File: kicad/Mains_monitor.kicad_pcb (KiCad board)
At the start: 2 copper layers, 69 x 89 mm, 35 parts, among them J1 Screw_Terminal_01x02, J2 Screw_Terminal_01x02, K1 SANYOU_SRD_Form_C, Q1 NPN, U1 HLW8032

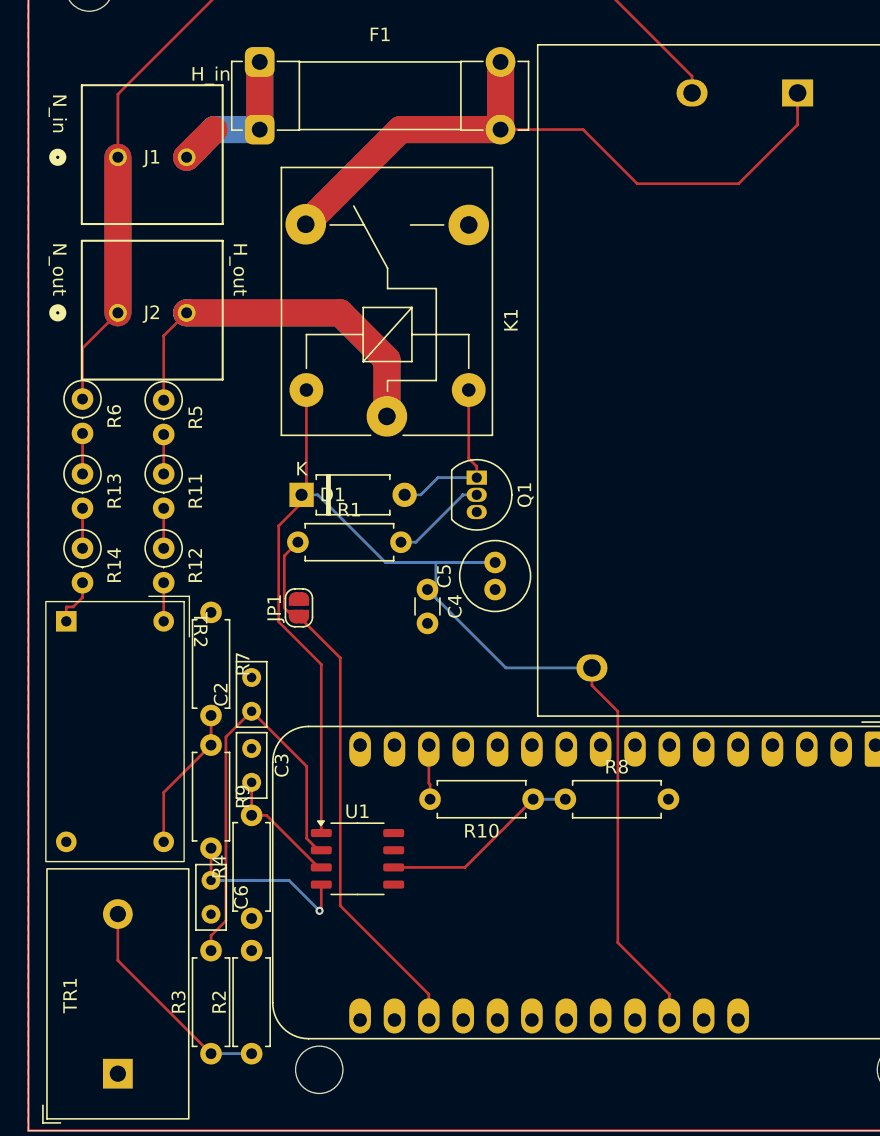
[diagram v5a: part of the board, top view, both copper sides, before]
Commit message: added updated screw terminal footprints
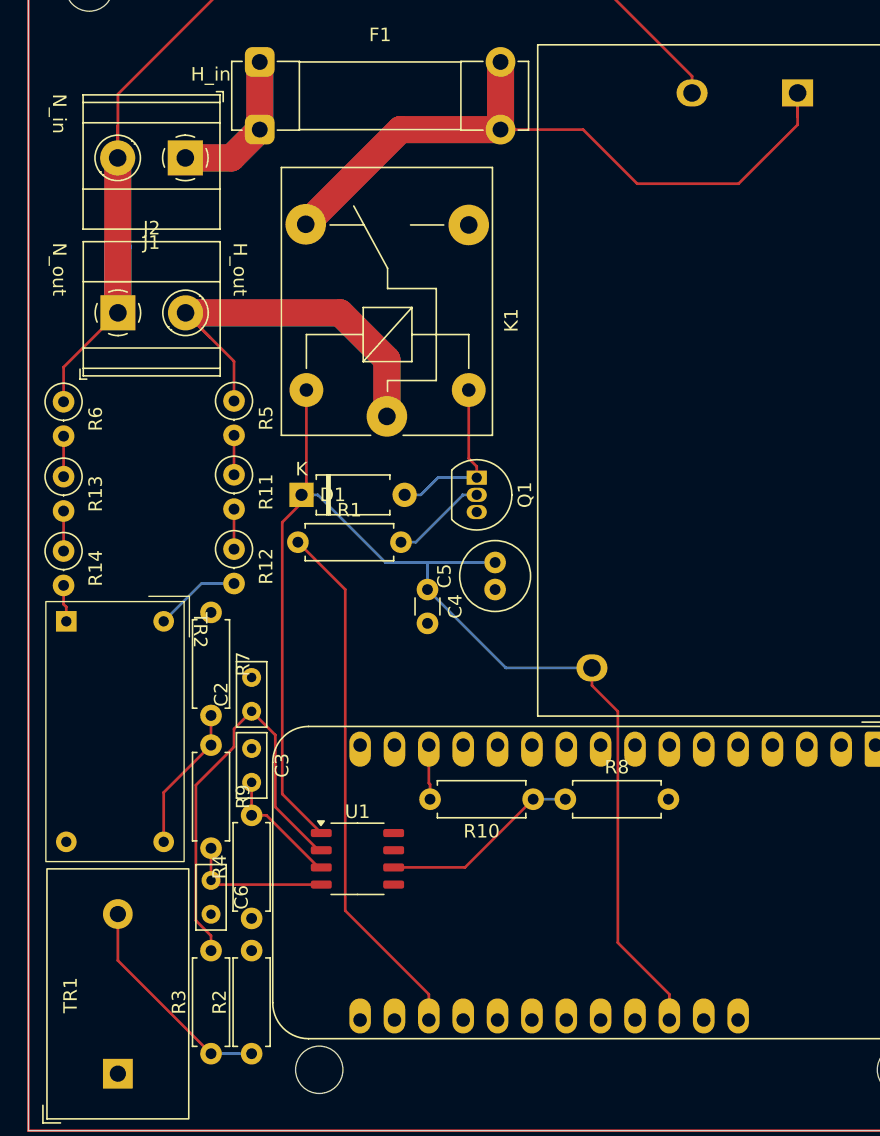
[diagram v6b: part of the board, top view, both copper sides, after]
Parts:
- removed JP1: RELAY LOGIC BYPASS, Jumper:SolderJumper-2_P1.3mm_Open_RoundedPad1.0x1.5mm
- J1, J2: footprint Connector_Screw_Terminal:CONN2_020000_WED -> TerminalBlock_Phoenix:TerminalBlock_Phoenix_MKDS-1,5-2_1x02_P5.00mm_Horizontal
- moved R11 5.20 mm to (105.7, 85.5)
- moved R12 5.20 mm to (105.7, 91.0)
- moved R5 5.20 mm to (105.7, 80.1)
- moved J1 4.99 mm to (102.1, 62.1), turned to 180 degrees
- moved R13 1.41 mm to (93.1, 85.7)
- moved R14 1.41 mm to (93.1, 91.2)
- moved R6 1.41 mm to (93.1, 80.1)
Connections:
- F1 pad 1: Net-(J1-Pin_2) -> Net-(J1-Pin_1)
- J1 pad 1: AC_N -> Net-(J1-Pin_1)
- J1 pad 2: Net-(J1-Pin_2) -> AC_N
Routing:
- net Net-(J1-Pin_1): track 0.00 -> 22.7 mm
- net Net-(J1-Pin_2): track 22.0 -> 0.00 mm
- net AC_N: track 85.5 -> 94.3 mm
- net Net-(R12-Pad2): track 2.85 -> 6.36 mm
- net RELAY_OUT: track 49.2 -> 52.6 mm
- net VP: track 13.3 -> 10.7 mm, vias 1 -> 0
- net AC_H: track 73.5 -> 75.3 mm
- net /RLY_CTRL: track 40.4 -> 39.3 mm
- net IP: track 31.5 -> 32.4 mm
- net Net-(R14-Pad2): track 3.65 -> 2.74 mm
- net +5V: track 97.5 -> 96.6 mm

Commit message: Clear DRC
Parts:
- Q1: value NPN -> Q_NPN_CBE; footprint Package_TO_SOT_THT:TO-92_Inline -> Package_TO_SOT_THT:TO-92
- moved H1 0.56 mm to (95.2, 50.0)
- moved C6 0.50 mm to (104.0, 116.0)
- moved R3 0.50 mm to (104.0, 128.8)
- moved R5 0.34 mm to (105.7, 80.4)
- moved R6 0.34 mm to (93.1, 80.5)
- moved Q1 0.25 mm to (123.8, 86.0)
- moved R7 0.25 mm to (104.0, 95.9)
- moved R11 0.23 mm to (105.7, 85.8)
- moved R9 0.19 mm to (104.0, 105.7)
- moved R13 0.09 mm to (93.1, 85.8)
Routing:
- net AC_N: track 94.3 -> 87.0 mm
- net IP: track 32.4 -> 28.5 mm
- net AC_H: track 75.3 -> 72.4 mm
- net RELAY_OUT: track 52.6 -> 50.1 mm
- net Net-(Q1-B): track 7.08 -> 8.33 mm

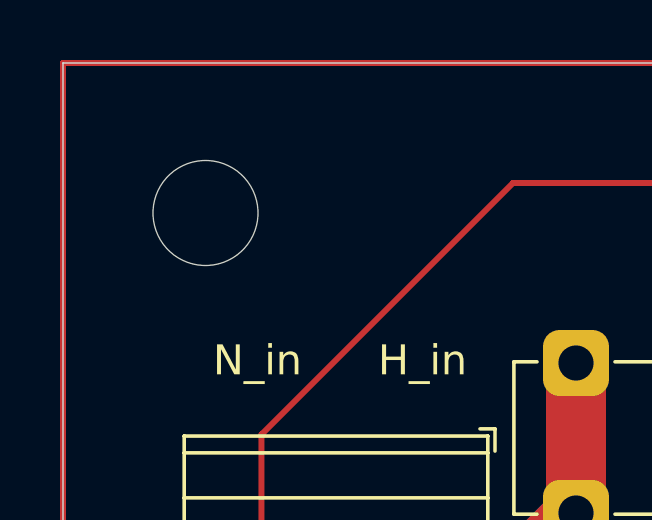
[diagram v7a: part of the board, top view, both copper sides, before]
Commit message: updated electrical spacing
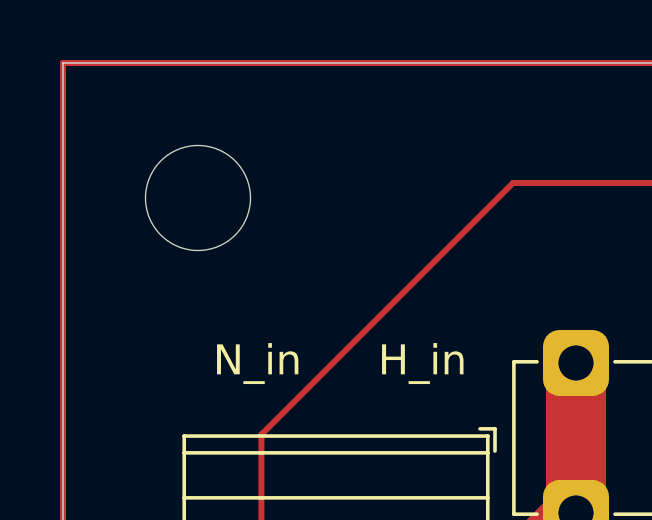
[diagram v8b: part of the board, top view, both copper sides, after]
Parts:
- moved H1 0.56 mm to (95.0, 49.5)
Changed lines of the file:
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@@
 	(footprint "MountingHole:MountingHole_3.5mm"
 		(layer "F.Cu")
-		(at 95.25 50)
+		(at 95 49.5)
 		(descr "Mounting Hole 3.5mm, no annular")
 		(tags "mounting hole 3.5mm no annular")
